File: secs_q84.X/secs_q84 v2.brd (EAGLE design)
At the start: 78.4 x 80 mm, 51 parts, among them IC1 MAX203ECWP, IC4 PIC18F47Q84-I_PT

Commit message: u[p
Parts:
- added SV2: CANBUS, con-lstb:MA06-1
- moved ZENER 54.8 mm to (58.4, 63.5)
- moved TP2 35.9 mm to (96.5, 33.0)
- moved TTL_SERIAL 35.3 mm to (47.0, 25.4), turned to 0 degrees
- moved R15 34.1 mm to (63.5, 31.8)
- moved R14 33.5 mm to (63.5, 26.7)
- moved RESET 31.8 mm to (25.4, 74.9)
- moved R3 30.7 mm to (71.1, 31.8)
- moved R7 30.2 mm to (30.5, 30.5), flipped to the bottom
- moved R4 30.1 mm to (71.1, 26.7)
- moved C5 29.6 mm to (86.4, 29.2)
- moved OS1_10MHZ 29.6 mm to (86.4, 29.2)
- moved R9 28.2 mm to (35.6, 30.5), flipped to the bottom
- moved LED1 28.1 mm to (30.5, 34.3)
- moved R19 27.9 mm to (35.6, 27.9), flipped to the bottom
- moved LED4 27.7 mm to (38.1, 34.3)
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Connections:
- net PVP_A renamed RS232_TX_OUT
- removed net PVP_B: A+REV.1, B-NORM.1, PVP_0.7
- new net RS232_RX_IN: A+REV.1, B-NORM.1, PVP_0.4
- net CANRX: now also SV2.2
- net CANTX: now also SV2.3
- net DERE: now also SV2.4
- net VCC: now also C2.1
- net VDD: now also SV2.5; no longer C2.1
- net VSS: now also SV2.1
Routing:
- net AN0: track 27.6 -> 107.6 mm, vias 0 -> 11
- net CANTX: track 0.00 -> 73.6 mm
- net CANRX: track 0.00 -> 69.9 mm, vias 0 -> 3
- net AN5: track 63.4 -> 117.3 mm, vias 4 -> 14
- net RELAY: track 23.3 -> 77.1 mm, vias 1 -> 11
- net DLED: track 99.9 -> 52.9 mm, vias 7 -> 5
- net PGD: track 88.3 -> 129.8 mm, vias 6 -> 12
- net PVP_B: track 40.8 -> 0.00 mm
- net DERE: track 25.2 -> 65.0 mm, vias 2 -> 4
- net PC_TX2: track 75.5 -> 39.9 mm, vias 6 -> 3
- net RS232_RX_IN: track 0.00 -> 35.0 mm
- net RD5: track 86.9 -> 53.6 mm, vias 0 -> 4
- net MLED: track 46.8 -> 15.5 mm, vias 0 -> 1
- net RE2: track 42.9 -> 70.9 mm, vias 2 -> 7
- net R_RESET: track 58.2 -> 85.8 mm, vias 5 -> 7
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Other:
- board size 78.4 x 80 mm -> 78.4 x 58.4 mm

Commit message: up
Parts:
- moved C10 36.4 mm to (71.1, 34.3)
- moved LED4 9.25 mm to (35.6, 25.4), turned to 270 degrees
- moved TTL_SERIAL 1.80 mm to (48.3, 24.1)
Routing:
- net CANTX: track 73.6 -> 211.9 mm, vias 0 -> 4
- net RB5: track 86.3 -> 16.2 mm, vias 9 -> 1
- net AN0: track 107.6 -> 43.4 mm, vias 11 -> 4
- net RELAY: track 77.1 -> 29.1 mm, vias 11 -> 2
- net PGD: track 129.8 -> 87.0 mm, vias 12 -> 14
- net RE2: track 70.9 -> 32.3 mm, vias 7 -> 0
- net VDD: track 304.7 -> 339.7 mm, vias 13 -> 21
- net MCLR_SIG: track 104.6 -> 77.7 mm, vias 10 -> 6
- net SDO1: track 97.7 -> 120.8 mm, vias 11 -> 10
- net CS: track 98.2 -> 118.7 mm, vias 9 -> 7
- net VREF: track 32.0 -> 52.1 mm, vias 0 -> 4
- net VCC: track 70.6 -> 51.8 mm, vias 5 -> 2
- net AN5: track 117.3 -> 135.4 mm, vias 14 -> 6
- net CLOCKO: track 67.3 -> 50.7 mm, vias 10 -> 0
- net AN2: track 94.1 -> 109.8 mm, vias 11 -> 14
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
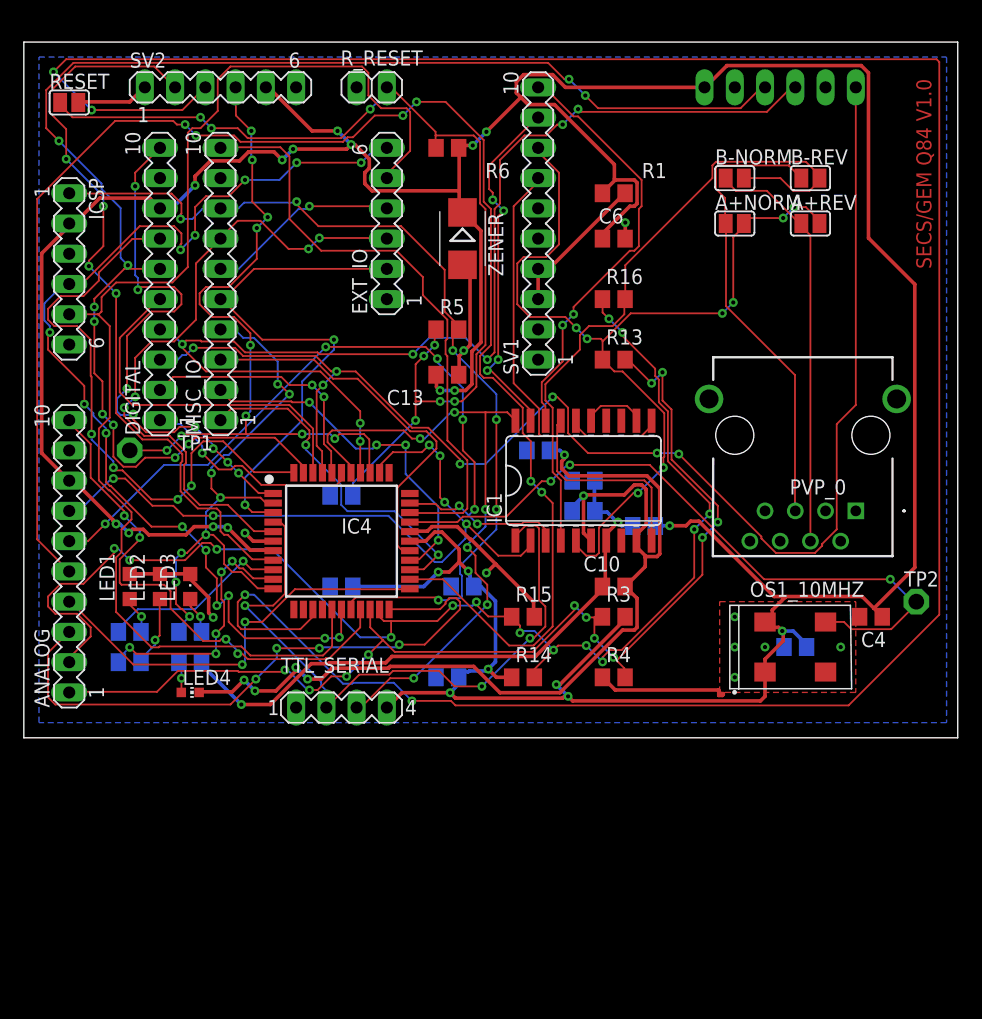
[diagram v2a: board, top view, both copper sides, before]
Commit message: two layer board
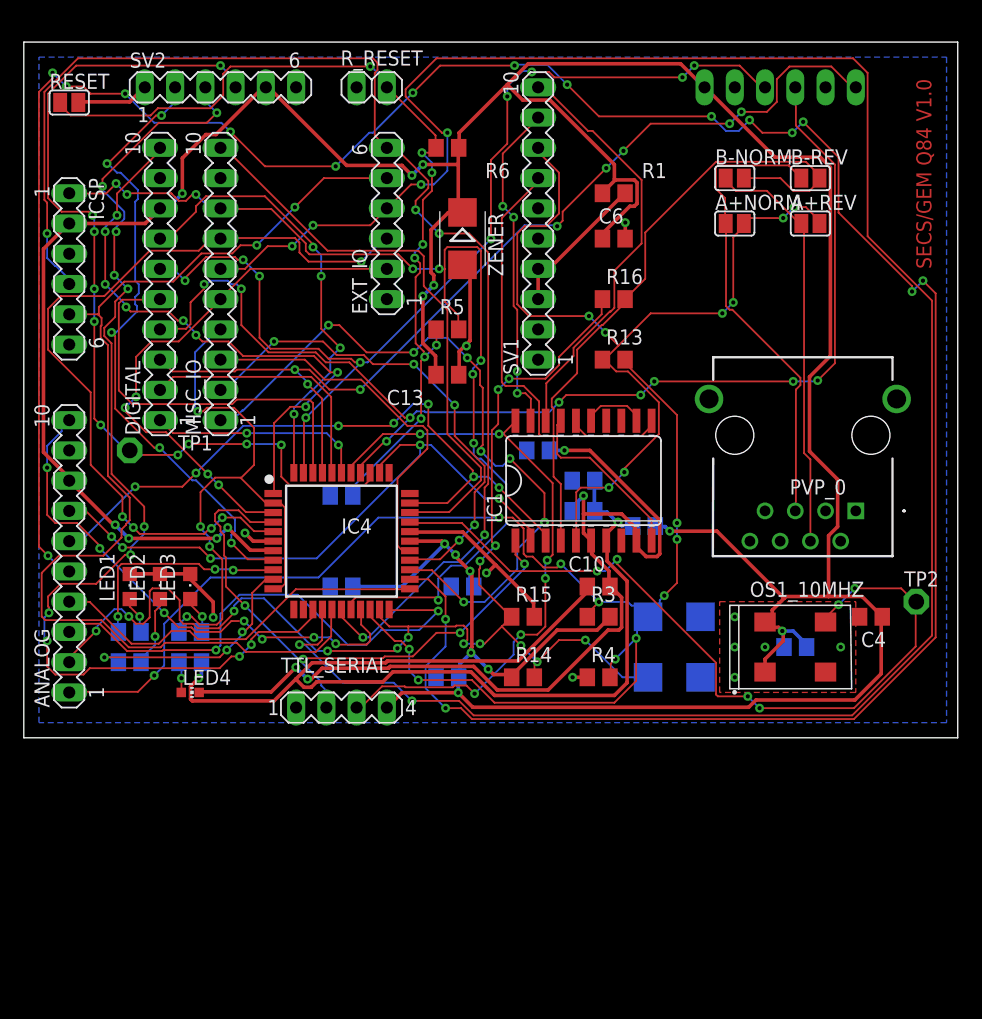
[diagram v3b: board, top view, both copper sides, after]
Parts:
- added D1, D2: 5.6V, diode:SMB
- moved C10 1.27 mm to (69.8, 34.3)
- moved R3 1.27 mm to (69.8, 31.8)
- moved R4 1.27 mm to (69.8, 26.7)
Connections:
- net AN1: now also D1.C
- net AN2: now also D2.C
- net VSS: now also D1.A, D2.A
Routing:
- net RB5: track 16.2 -> 183.9 mm, vias 1 -> 6
- net CANTX: track 211.9 -> 90.4 mm, vias 4 -> 11
- net AN5: track 135.4 -> 225.4 mm, vias 6 -> 17
- net VCC: track 51.8 -> 91.9 mm
- net CS: track 118.7 -> 82.8 mm, vias 7 -> 8
- net SDO1: track 120.8 -> 88.3 mm
- net RELAY: track 29.1 -> 60.6 mm, vias 2 -> 7
- net AN1: track 94.2 -> 125.6 mm, vias 12 -> 11
- net PGD: track 87.0 -> 109.9 mm, vias 14 -> 5
- net DERE: track 60.7 -> 76.6 mm
- net PGC: track 105.8 -> 92.2 mm, vias 0 -> 2
- net RD7: track 53.9 -> 67.4 mm, vias 4 -> 5
- net UC_TX: track 49.9 -> 38.0 mm
- net MISC: track 30.0 -> 41.7 mm, vias 4 -> 5
- net CANRX: track 63.7 -> 52.8 mm, vias 4 -> 5
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
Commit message: up
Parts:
- added F1: 0805L075WR, 0805L075WR:FUSC2114X125N
- added GLORY: GLORY, pinhead:1X02
- moved R13 11.4 mm to (71.1, 64.8)
- moved R16 10.2 mm to (71.1, 68.6)
- moved C6 8.89 mm to (71.1, 72.4)
- moved R1 8.89 mm to (71.1, 76.2)
- moved C10 8.13 mm to (76.2, 29.2)
- moved R15 8.13 mm to (69.8, 26.7)
- moved R4 6.84 mm to (63.5, 29.2)
- moved LED3 5.08 mm to (30.5, 34.3), turned to 90 degrees
- moved LED1 5.08 mm to (30.5, 39.4), turned to 90 degrees
- moved LED2 3.59 mm to (30.5, 36.8), turned to 90 degrees
- moved R3 2.54 mm to (69.8, 29.2)
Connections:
- new net POWERIN: F1.1, GLORY.2
- net VDD: now also F1.2
- net VSS: now also GLORY.1
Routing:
- net AN5: track 225.4 -> 41.2 mm, vias 17 -> 1
- net RB5: track 183.9 -> 55.7 mm, vias 6 -> 1
- net RS232TX: track 75.9 -> 116.4 mm, vias 8 -> 2
- net VCC: track 91.9 -> 62.8 mm, vias 2 -> 4
- net AN1: track 125.6 -> 98.2 mm, vias 11 -> 4
- net PGD: track 109.9 -> 84.4 mm, vias 5 -> 2
- net SCK1: track 99.2 -> 73.7 mm, vias 9 -> 1
- net RD7: track 67.4 -> 43.3 mm, vias 5 -> 1
- net MCLR_SIG: track 88.4 -> 109.9 mm, vias 9 -> 1
- net RS232RX: track 80.9 -> 99.8 mm
- net RELAY: track 60.6 -> 41.8 mm, vias 7 -> 1
- net R_RESET: track 75.7 -> 94.0 mm, vias 8 -> 2
- net CANTX: track 90.4 -> 74.7 mm, vias 11 -> 0
- net AN4: track 32.5 -> 48.0 mm, vias 0 -> 1
- net PC_RX2: track 54.1 -> 41.1 mm, vias 6 -> 2
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
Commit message: up
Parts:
- moved C11 3.81 mm to (48.3, 38.1)
- moved DISPLAY 1.27 mm to (83.8, 76.2)
- moved PVP_0 1.27 mm to (90.2, 40.6)
- flipped C6 to the bottom
- turned LED4 to 90 degrees
- flipped R1 to the bottom
- flipped R13 to the bottom
- flipped R16 to the bottom
- renumbered OS1_10MHZ to OS1_16MHZ
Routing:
- net RS232TX: track 116.4 -> 75.7 mm, vias 2 -> 3
- net VSS: track 51.8 -> 41.9 mm
- net VDD: track 332.8 -> 338.4 mm, vias 7 -> 8
- net AN2: track 107.8 -> 110.9 mm, vias 3 -> 4
- net GND: track 76.3 -> 78.8 mm, vias 5 -> 4
- net DPOWER: track 21.6 -> 20.1 mm
- net SDO1: track 89.8 -> 88.5 mm
- net CS: track 83.2 -> 82.1 mm
- net N$3: track 2.63 -> 3.42 mm
- net RS232RX: track 99.8 -> 100.5 mm, vias 0 -> 1
- net RS232_TX_OUT: track 39.3 -> 39.0 mm, vias 0 -> 1
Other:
- board text added: "SECS/GEM Q84 V1.1"
- board text removed: "SECS/GEM Q84 V1.0"

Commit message: up
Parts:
- removed D1, D2: 5.6V, diode:SMB
- added Z1, Z2: BZT52B5V6-TP, BZT52B5V6-TP:SOD3716X135N
- R13, R16: value 86.6k -> 82.5k
- moved R3 6.48 mm to (63.5, 30.5), turned to 180 degrees
- moved R4 6.48 mm to (69.8, 30.5), turned to 180 degrees
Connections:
- net AN1: now also Z1.1; no longer D1.C
- net AN2: now also Z2.1; no longer D2.C
- net VSS: now also Z1.2, Z2.2; no longer D1.A, D2.A
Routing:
- net VDD: track 338.4 -> 347.5 mm
- net AN2: track 110.9 -> 112.5 mm
- net AN1: track 98.1 -> 99.6 mm
